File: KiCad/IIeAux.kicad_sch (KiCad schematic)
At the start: 15 parts, among them J1 Aux Slot, U1 SN74LVC245AN, U2 TangNano9K, U3 74LS245, U4 74LS374, U5 SN74LVC245AN, U6 SN74LVC245AN

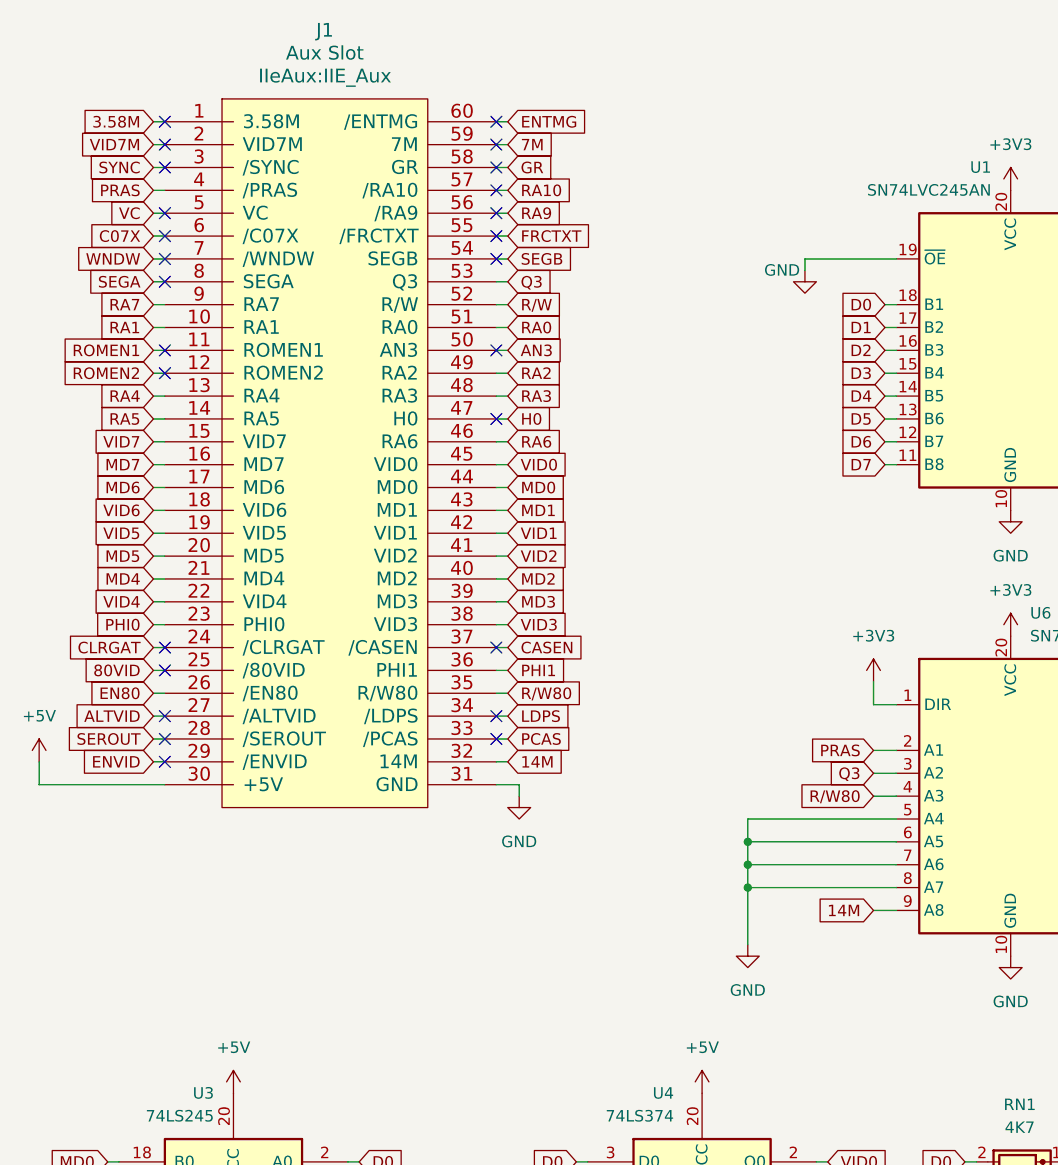
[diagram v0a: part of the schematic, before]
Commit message: DVI output 560 x 192
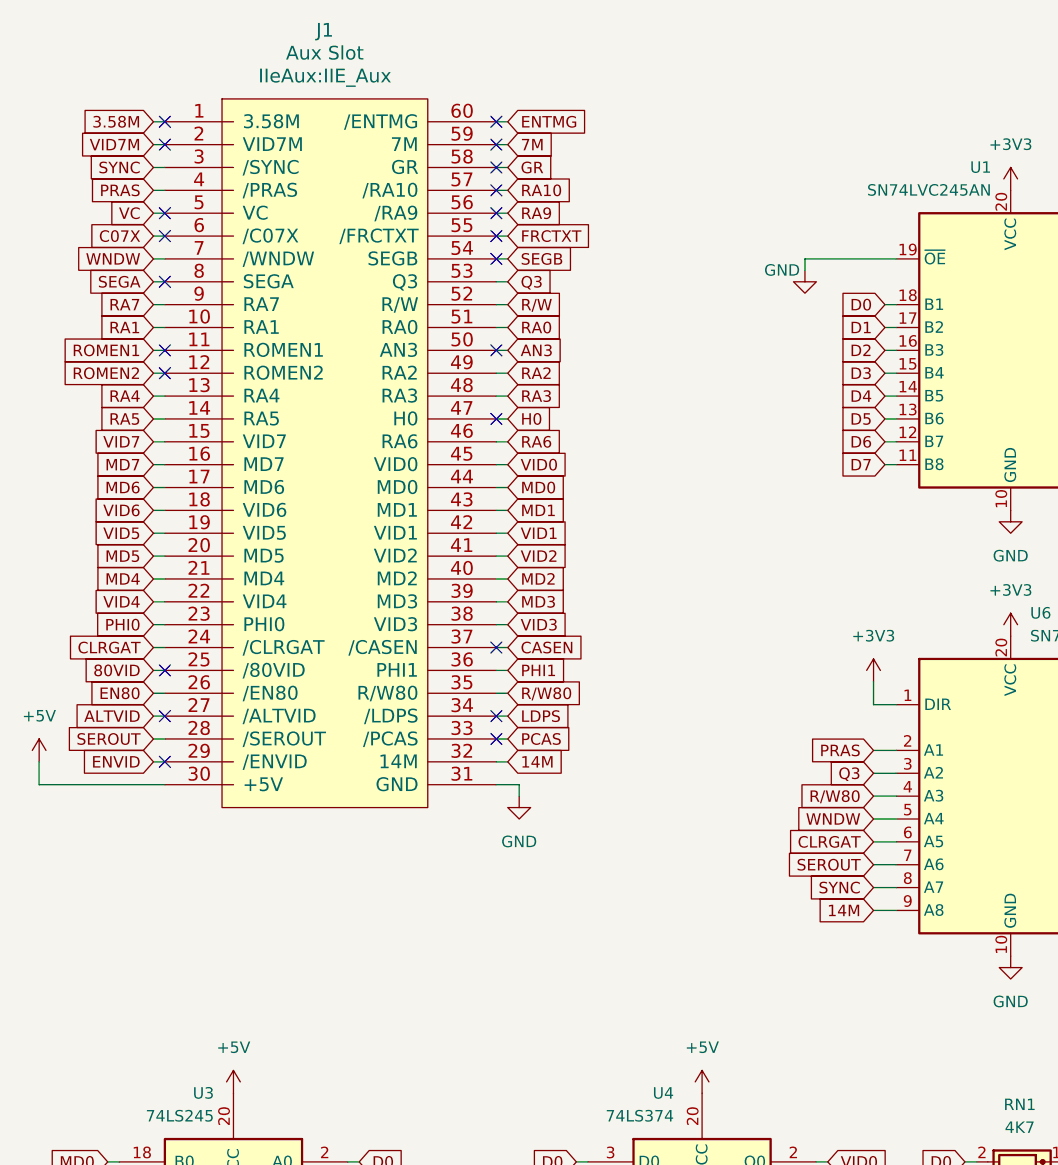
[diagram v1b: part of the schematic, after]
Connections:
- net CLRGAT: now also U6.6 (A5)
- net GND: no longer U6.5 (A4), U6.6 (A5), U6.7 (A6), U6.8 (A7)
- net SEROUT: now also U6.7 (A6)
- net SYNC: now also U6.8 (A7)
- net WNDW: now also U6.5 (A4)
- no-connect marks 47 -> 43
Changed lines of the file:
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@@
 		(title "IIeAux")
 		(date "2026-03-07")
-		(rev "1.0.2")
+		(rev "1.0.3")
 		(company "nanja.info")
 		(comment 1 "Apple IIe Aux Slot FPGA Card")
 		(comment 2 "80 Column Text")
+		(comment 3 "Input video signals")
 	)
 	(junction
@@
 	)
 	(junction
-		(at 106.68 114.3)
-		(diameter 0)
-		(color 0 0 0 0)
-	)
-	(junction
 		(at 180.34 149.86)
 		(diameter 0)
@@
 	)
 	(junction
-		(at 106.68 116.84)
-		(diameter 0)
-		(color 0 0 0 0)
-	)
-	(junction
-		(at 106.68 111.76)
-		(diameter 0)
-		(color 0 0 0 0)
-	)
-	(junction
 		(at 217.17 142.24)
 		(diameter 0)
@@
 	)
 	(no_connect
-		(at 41.91 90.17)
-	)
-	(no_connect
 		(at 41.91 49.53)
 	)
@@
 	)
 	(no_connect
-		(at 41.91 36.83)
-	)
-	(no_connect
 		(at 210.82 72.39)
 	)
@@
 	)
 	(no_connect
-		(at 41.91 46.99)
-	)
-	(no_connect
 		(at 210.82 92.71)
 	)
@@
 	)
 	(no_connect
-		(at 41.91 100.33)
-	)
-	(no_connect
 		(at 210.82 95.25)
 	)
@@
 	(wire
 		(pts
+			(xy 120.65 109.22) (xy 123.19 109.22)
+		)
+		(stroke
+			(width 0)
+			(type default)
+		)
+	)
+	(wire
+		(pts
 			(xy 78.74 74.93) (xy 80.01 74.93)
 		)
@@
 	(wire
 		(pts
-			(xy 106.68 116.84) (xy 106.68 123.19)
-		)
-		(stroke
-			(width 0)
-			(type default)
-		)
-	)
-	(wire
-		(pts
 			(xy 40.64 59.69) (xy 41.91 59.69)
 		)
@@
 	(wire
 		(pts
-			(xy 106.68 109.22) (xy 106.68 111.76)
-		)
-		(stroke
-			(width 0)
-			(type default)
-		)
-	)
-	(wire
-		(pts
 			(xy 62.23 172.72) (xy 63.5 172.72)
 		)
@@
 	(wire
 		(pts
-			(xy 106.68 111.76) (xy 106.68 114.3)
+			(xy 262.89 46.99) (xy 261.62 46.99)
 		)
 		(stroke
@@
 	(wire
 		(pts
-			(xy 262.89 46.99) (xy 261.62 46.99)
+			(xy 120.65 111.76) (xy 123.19 111.76)
 		)
 		(stroke
@@
 	(wire
 		(pts
+			(xy 120.65 114.3) (xy 123.19 114.3)
+		)
+		(stroke
+			(width 0)
+			(type default)
+		)
+	)
+	(wire
+		(pts
 			(xy 210.82 97.79) (xy 213.36 97.79)
 		)
@@
 	(wire
 		(pts
-			(xy 106.68 114.3) (xy 106.68 116.84)
-		)
-		(stroke
-			(width 0)
-			(type default)
-		)
-	)
-	(wire
-		(pts
 			(xy 78.74 85.09) (xy 80.01 85.09)
 		)
@@
 	(wire
 		(pts
+			(xy 120.65 116.84) (xy 123.19 116.84)
+		)
+		(stroke
+			(width 0)
+			(type default)
+		)
+	)
+	(wire
+		(pts
 			(xy 35.56 162.56) (xy 36.83 162.56)
 		)
@@
 	(wire
 		(pts
-			(xy 106.68 111.76) (xy 123.19 111.76)
-		)
-		(stroke
-			(width 0)
-			(type default)
-		)
-	)
-	(wire
-		(pts
 			(xy 78.74 34.29) (xy 80.01 34.29)
 		)
@@
 	(wire
 		(pts
-			(xy 106.68 116.84) (xy 123.19 116.84)
-		)
-		(stroke
-			(width 0)
-			(type default)
-		)
-	)
-	(wire
-		(pts
-			(xy 106.68 114.3) (xy 123.19 114.3)
-		)
-		(stroke
-			(width 0)
-			(type default)
-		)
-	)
-	(wire
-		(pts
 			(xy 120.65 93.98) (xy 120.65 96.52)
 		)
@@
 	(wire
 		(pts
-			(xy 106.68 109.22) (xy 123.19 109.22)
-		)
-		(stroke
-			(width 0)
-			(type default)
-		)
-	)
-	(wire
-		(pts
 			(xy 214.63 76.2) (xy 215.9 76.2)
 		)
@@
 		)
 	)
+	(global_label "SYNC"
+		(shape input)
+		(at 120.65 116.84 180)
+		(fields_autoplaced yes)
+		(effects
+			(font
+				(size 1.27 1.27)
+			)
+			(justify right)
+		)
+		(property "Intersheetrefs" "${INTERSHEET_REFS}"
+			(at 112.7662 116.84 0)
+			(effects
+				(font
+					(size 1.27 1.27)
+				)
+				(justify right)
+				(hide yes)
+			)
+		)
+	)
 	(global_label "Q3"
 		(shape input)
@@
 		)
 	)
+	(global_label "SEROUT"
+		(shape input)
+		(at 120.65 114.3 180)
+		(fields_autoplaced yes)
+		(effects
+			(font
+				(size 1.27 1.27)
+			)
+			(justify right)
+		)
+		(property "Intersheetrefs" "${INTERSHEET_REFS}"
+			(at 110.4077 114.3 0)
+			(effects
+				(font
+					(size 1.27 1.27)
+				)
+				(justify right)
+				(hide yes)
+			)
+		)
+	)
 	(global_label "MD6"
 		(shape input)
@@
 		)
 	)
+	(global_label "WNDW"
+		(shape input)
+		(at 120.65 109.22 180)
+		(fields_autoplaced yes)
+		(effects
+			(font
+				(size 1.27 1.27)
+			)
+			(justify right)
+		)
+		(property "Intersheetrefs" "${INTERSHEET_REFS}"
+			(at 112.1615 109.22 0)
+			(effects
+				(font
+					(size 1.27 1.27)
+				)
+				(justify right)
+				(hide yes)
+			)
+		)
+	)
 	(global_label "VID4"
 		(shape input)
@@
 		)
 	)
+	(global_label "CLRGAT"
+		(shape input)
+		(at 120.65 111.76 180)
+		(fields_autoplaced yes)
+		(effects
+			(font
+				(size 1.27 1.27)
+			)
+			(justify right)
+		)
+		(property "Intersheetrefs" "${INTERSHEET_REFS}"
+			(at 110.7705 111.76 0)
+			(effects
+				(font
+					(size 1.27 1.27)
+				)
+				(justify right)
+				(hide yes)
+			)
+		)
+	)
 	(global_label "RA0"
 		(shape input)
@@
 					(unit 1)
 				)
-			)
-		)
-	)
-	(symbol
-		(lib_id "IIeAux:GND")
-		(at 106.68 123.19 0)
-		(unit 1)
-		(exclude_from_sim no)
-		(in_bom yes)
-		(on_board yes)
-		(dnp no)
-		(fields_autoplaced yes)
-		(property "Reference" "#PWR07"
-			(at 106.68 129.54 0)
-			(effects
-				(font
-					(size 1.27 1.27)
-				)
-				(hide yes)
-			)
-		)
-		(property "Value" "GND"
-			(at 106.68 128.27 0)
-			(effects
-				(font
-					(size 1.27 1.27)
-				)
-			)
-		)
-		(property "Footprint" ""
-			(at 106.68 123.19 0)
-			(effects
-				(font
-					(size 1.27 1.27)
-				)
-				(hide yes)
-			)
-		)
-		(property "Datasheet" ""
-			(at 106.68 123.19 0)
-			(effects
-				(font
-					(size 1.27 1.27)
-				)
-				(hide yes)
-			)
-		)
-		(property "Description" "Power symbol creates a global label with name \"GND\" , ground"
-			(at 106.68 123.19 0)
-			(effects
-				(font
-					(size 1.27 1.27)
-				)
-				(hide yes)
-			)
-		)
-		(pin "1"
-		)
-		(instances
-			(project "IIeAux"
-				(path "/9f1db0d4-0fbb-436a-b3be-9c0e5dc61ef0"
-					(reference "#PWR07")
-					(unit 1)
-				)
